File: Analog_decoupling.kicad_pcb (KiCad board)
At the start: 2 copper layers, 188.1 x 142 mm, 131 parts, among them J1 22-23-2021, J2 22-23-2021, J3 22-23-2021, J4 302-S101, J5 OSTTC020162, U1 LT1129CST-5#PBF, U10 TLV9001IDBVR, U11 TLV9001IDBVR, U12 LP2985A-50DBVR, U13 LP2985A-50DBVR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

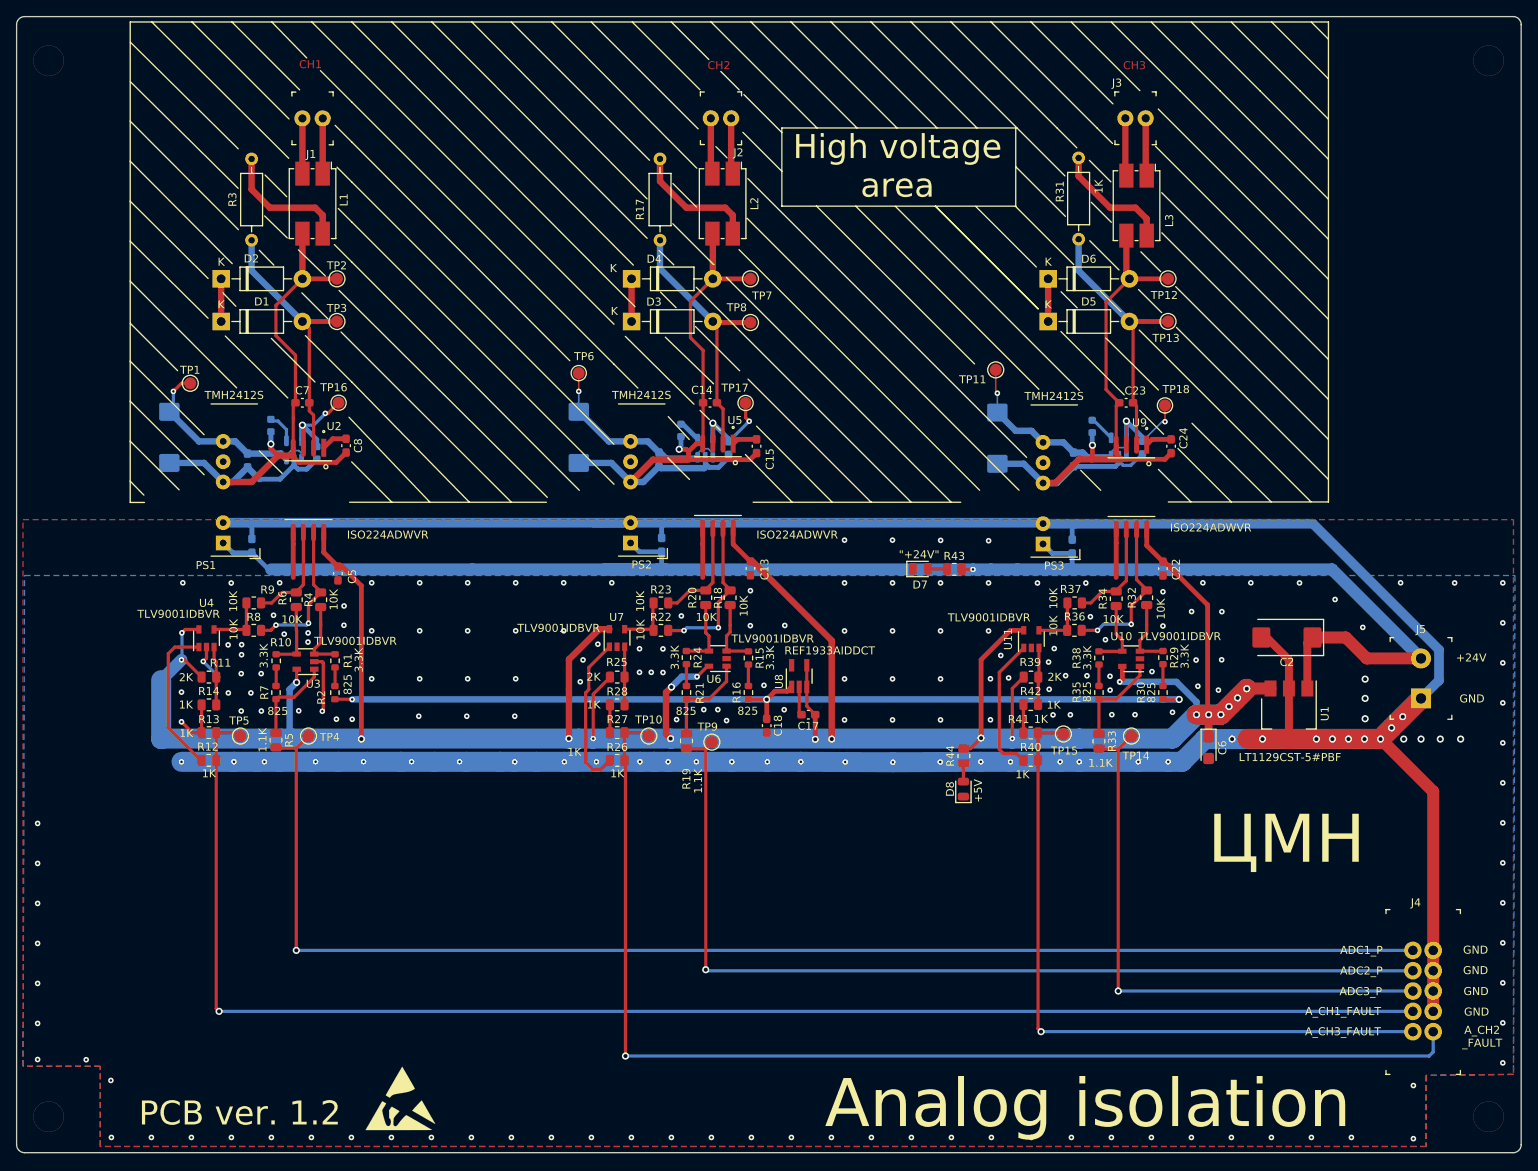
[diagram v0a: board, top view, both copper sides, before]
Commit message: Analog decoupling PCB J4 and J5 moved to left edge
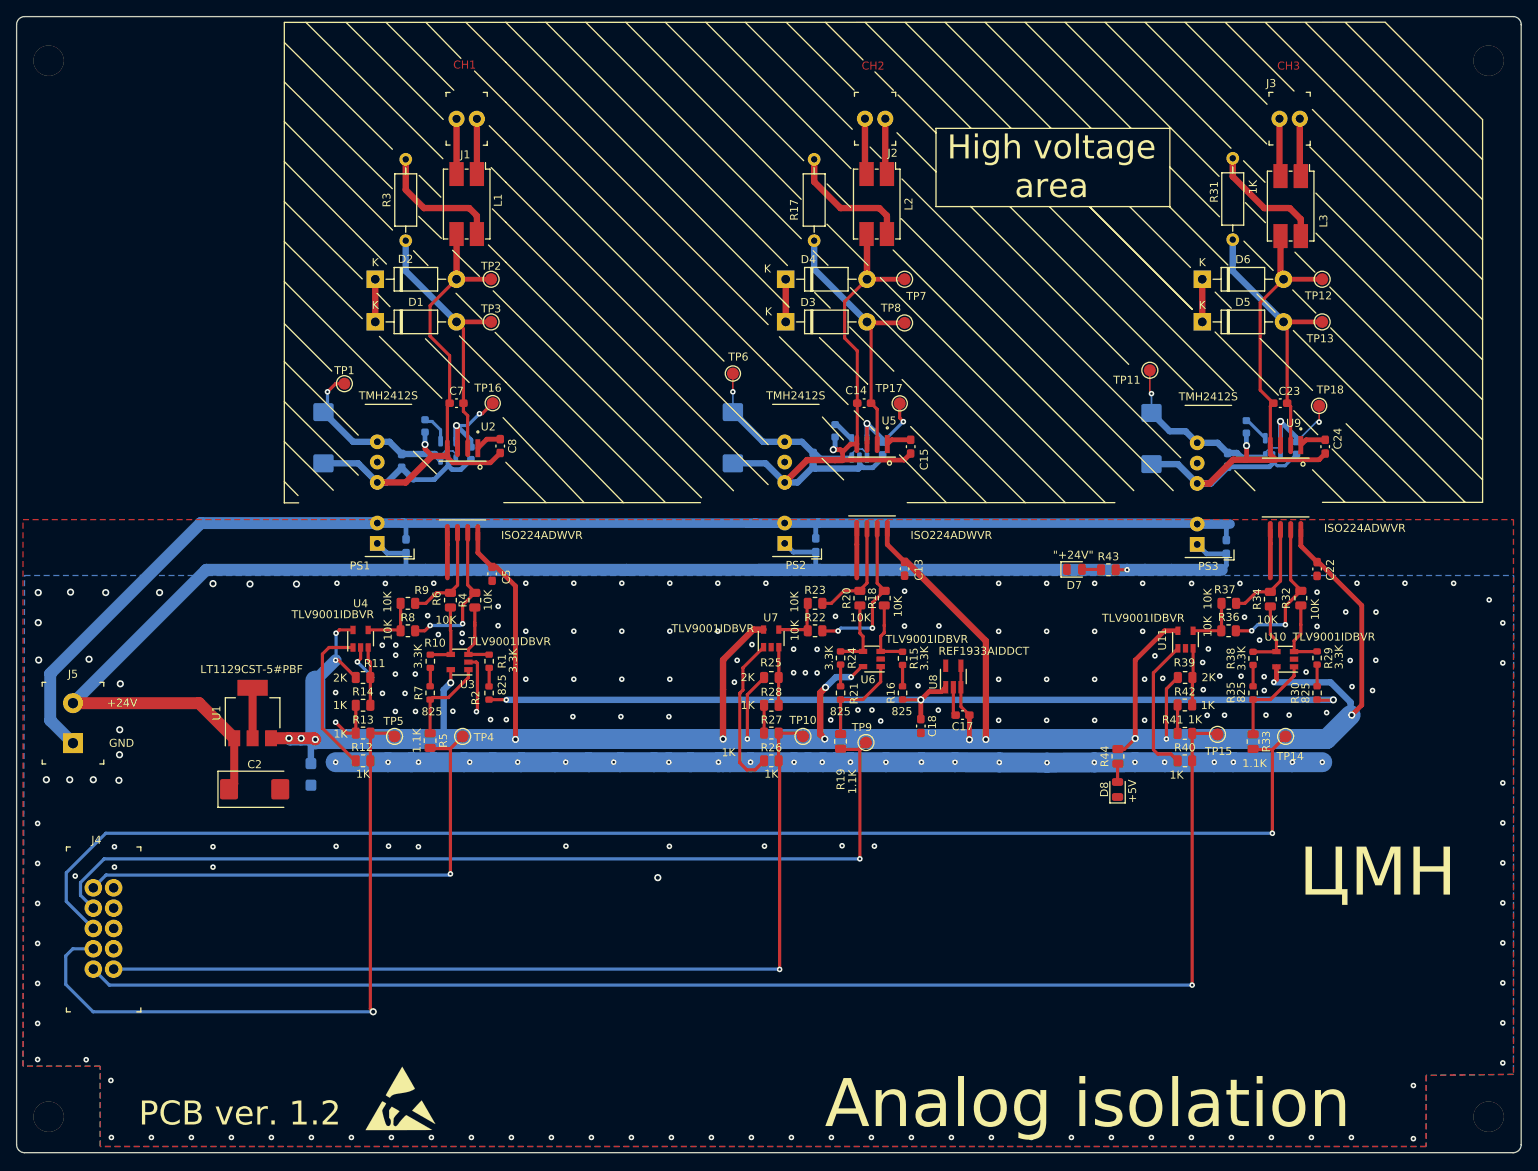
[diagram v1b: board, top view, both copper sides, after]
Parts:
- C6: moved to B.Cu
- moved J5 168.6 mm to (70.5, 141.6)
- moved J4 165.1 mm to (75.6, 159.7)
- moved C2 130.4 mm to (93.2, 147.4), turned to 0 degrees
- moved U1 129.5 mm to (93.0, 137.8), turned to 90 degrees
- moved C6 112.3 mm to (100.3, 145.5)
- moved C12 19.3 mm to (153.0, 103.4)
- moved C13 19.3 mm to (174.5, 119.8)
- moved C15 19.3 mm to (175.2, 104.5)
- moved C17 19.3 mm to (181.7, 138.1)
- moved C19 19.3 mm to (214.7, 117.1)
- moved C24 19.3 mm to (227.0, 104.5)
- moved C26 19.3 mm to (171.7, 104.8)
- moved C27 19.3 mm to (217.2, 102.1)
- moved C28 19.3 mm to (223.5, 104.7)
- moved D7 19.3 mm to (195.7, 119.9)
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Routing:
- net /ADC3_P: track 71.8 -> 176.4 mm
- net GNDREF: track 457.2 -> 353.1 mm, vias 212 -> 217
- net /ADC1_P: track 169.5 -> 65.7 mm
- net /A_CH1_FAULT: track 187.4 -> 85.4 mm
- net /A_CH3_FAULT: track 87.1 -> 172.8 mm
- net /A_CH2_FAULT: track 147.4 -> 116.0 mm
- net +24V: track 195.4 -> 203.8 mm
- net +5V_Analog: track 357.3 -> 349.1 mm, vias 20 -> 18
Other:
- board text added: "Scheema and PCB designed by SVIELCOM"
- board text removed: "ADC1_P"
- board text removed: "ADC2_P"
- board text removed: "ADC3_P"
- board text removed: "A_CH1_FAULT"
- board text removed: "A_CH2 _FAULT"
- board text removed: "A_CH3_FAULT"
- board text removed: "Schema and PCB designed by SVIELCOM"

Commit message: minor changes
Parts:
- moved J4 4.98 mm to (80.6, 159.6)
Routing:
- net /A_CH2_FAULT: track 116.0 -> 109.8 mm
- net /ADC1_P: track 65.7 -> 60.8 mm
- net /A_CH3_FAULT: track 172.8 -> 170.7 mm
- net /ADC2_P: track 119.8 -> 117.9 mm
- net /ADC3_P: track 176.4 -> 178.1 mm
- net /A_CH1_FAULT: track 85.4 -> 84.5 mm
- net GNDREF: vias 217 -> 238
- net (no net): vias 0 -> 3

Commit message: GPIO port changed for input signals
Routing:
- net GNDREF: vias 238 -> 241
- net (no net): vias 3 -> 0
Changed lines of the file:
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@@
     (property "Status" "Active")
     (attr through_hole)
-    (fp_text reference "J1" (at 1.45 -4.48) (layer "F.SilkS")
+    (fp_text reference "J1" (at -2.9083 0.1143) (layer "F.SilkS")
       (effects (font (size 1 1) (thickness 0.15)))
     )
@@
       (effects (font (size 1 1) (thickness 0.15)))
     )
-    (fp_text user "${REFERENCE}" (at 1.25 0.03) (layer "F.Fab")
+    (fp_text user "${REFERENCE}" (at 1.3335 1.9939) (layer "F.Fab") hide
       (effects (font (size 1 1) (thickness 0.15)))
     )
@@
       (effects (font (size 1 1) (thickness 0.15)))
     )
-    (fp_text user "${REFERENCE}" (at 1.25 0.03) (layer "F.Fab")
+    (fp_text user "${REFERENCE}" (at -2.5273 -1.8796) (layer "F.SilkS")
       (effects (font (size 1 1) (thickness 0.15)))
     )
@@
     (property "Status" "Active")
     (attr through_hole)
-    (fp_text reference "J2" (at -0.9144 -4.2926) (layer "F.SilkS")
+    (fp_text reference "J2" (at -2.5273 -0.127) (layer "F.SilkS")
       (effects (font (size 1 1) (thickness 0.15)))
     )
@@
       (effects (font (size 1 1) (thickness 0.15)))
     )
-    (fp_text user "${REFERENCE}" (at 1.25 0.508) (layer "F.Fab")
+    (fp_text user "${REFERENCE}" (at 1.25 0.508) (layer "F.Fab") hide
       (effects (font (size 1 1) (thickness 0.15)))
     )
@@
     (property "Sheetname" "")
     (attr smd)
-    (fp_text reference "U14" (at 2.9519 -1.1074 180) (layer "B.SilkS")
+    (fp_text reference "U14" (at -2.4583 3.8075 180) (layer "B.SilkS")
       (effects (font (size 1 1) (thickness 0.15)) (justify mirror))
     )
@@
     (property "Sheetname" "")
     (attr smd)
-    (fp_text reference "U13" (at 3.9171 -0.828 180) (layer "B.SilkS")
+    (fp_text reference "U13" (at -2.2043 4.3917 180) (layer "B.SilkS")
       (effects (font (size 1 1) (thickness 0.15)) (justify mirror))
     )
@@
     (property "Sheetname" "")
     (attr smd)
-    (fp_text reference "U12" (at 4.2219 -0.6096 180) (layer "B.SilkS")
+    (fp_text reference "U12" (at -1.8487 7.9629 180) (layer "B.SilkS")
       (effects (font (size 1 1) (thickness 0.15)) (justify mirror))
     )
@@
     (effects (font (size 1 1) (thickness 0.15)))
   )
-  (via (at 75.8952 163.449) (size 0.7) (drill 0.3) (layers "F.Cu" "B.Cu") (free) (net 0))
-  (via (at 73.2282 166.4462) (size 0.7) (drill 0.3) (layers "F.Cu" "B.Cu") (free) (net 0))
-  (via (at 73.2028 159.2326) (size 0.7) (drill 0.3) (layers "F.Cu" "B.Cu") (free) (net 0))
   (segment (start 106.4641 131.0386) (end 106.0577 131.445) (width 0.4) (layer "F.Cu") (net 1))
   (segment (start 117.3099 115.333323) (end 117.3099 116.7638) (width 0.6) (layer "F.Cu") (net 1))
@@
   (via (at 76.4286 134.1882) (size 0.9) (drill 0.5) (layers "F.Cu" "B.Cu") (free) (net 1))
   (via (at 123.6472 126.9238) (size 0.7) (drill 0.3) (layers "F.Cu" "B.Cu") (net 1))
+  (via (at 75.8952 163.449) (size 0.7) (drill 0.3) (layers "F.Cu" "B.Cu") (free) (net 1))
   (via (at 231.013 121.6152) (size 0.7) (drill 0.3) (layers "F.Cu" "B.Cu") (net 1))
   (via (at 76.327 143.0528) (size 0.9) (drill 0.5) (layers "F.Cu" "B.Cu") (free) (net 1))
@@
   (via (at 219.6338 138.0998) (size 0.7) (drill 0.3) (layers "F.Cu" "B.Cu") (net 1))
   (via (at 110.8075 132.969) (size 0.7) (drill 0.3) (layers "F.Cu" "B.Cu") (net 1))
+  (via (at 73.2282 166.4462) (size 0.7) (drill 0.3) (layers "F.Cu" "B.Cu") (free) (net 1))
   (via (at 224.6503 132.715) (size 0.7) (drill 0.3) (layers "F.Cu" "B.Cu") (free) (net 1))
   (via (at 66.167 122.7836) (size 0.9) (drill 0.5) (layers "F.Cu" "B.Cu") (free) (net 1))
@@
   (via (at 106.0577 131.445) (size 0.7) (drill 0.3) (layers "F.Cu" "B.Cu") (net 1))
   (via (at 166.6494 154.432) (size 0.7) (drill 0.3) (layers "F.Cu" "B.Cu") (free) (net 1))
+  (via (at 73.2028 159.2326) (size 0.7) (drill 0.3) (layers "F.Cu" "B.Cu") (free) (net 1))
   (via (at 112.014 135.382) (size 0.7) (drill 0.3) (layers "F.Cu" "B.Cu") (net 1))
   (via (at 113.3221 137.6426) (size 0.7) (drill 0.3) (layers "F.Cu" "B.Cu") (net 1))
